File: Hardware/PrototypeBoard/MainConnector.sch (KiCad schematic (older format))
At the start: 13 parts, among them J3 ControlSupplyConnector

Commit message: Layout almost done
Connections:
- net ~GateDriverErr1: now also J3.9 (Pin_9); no longer J3.10 (Pin_10)
- net ~GateDriverErr2: now also J3.10 (Pin_10); no longer J3.9 (Pin_9)
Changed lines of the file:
@@
 Text HLabel 4500 2800 2    60   Output ~ 0
 GateDriverEna
+Text HLabel 3600 2700 0    60   Input ~ 0
+~GateDriverErr1
 Text HLabel 4500 2700 2    60   Input ~ 0
-~GateDriverErr1
-Text HLabel 3600 2700 0    60   Input ~ 0
 ~GateDriverErr2
 Text HLabel 4500 3200 2    60   Output ~ 0
@@
 	3800 4400 3700 4400
 Wire Wire Line
-	3700 4400 3700 5200
-Wire Wire Line
-	3600 4600 3800 4600
+	3700 4400 3700 4500
+Wire Wire Line
+	3600 4600 3700 4600
 Wire Wire Line
 	3800 4500 3700 4500
@@
 Connection ~ 3700 4600
 Wire Wire Line
-	3600 2300 3800 2300
-Wire Wire Line
-	3700 1700 3700 2500
+	3600 2300 3700 2300
+Wire Wire Line
+	3700 1700 3700 2000
 Wire Wire Line
 	3800 2400 3700 2400
 Connection ~ 3700 2400
 Wire Wire Line
-	4300 4600 7200 4600
-Wire Wire Line
-	4400 4400 4400 5200
+	4300 4600 4400 4600
+Wire Wire Line
+	4400 4400 4400 4500
 Wire Wire Line
 	4300 4500 4400 4500
@@
 	4300 2400 4400 2400
 Wire Wire Line
-	4300 4300 6000 4300
-Wire Wire Line
-	4300 2600 6000 2600
+	4300 4300 5900 4300
+Wire Wire Line
+	4300 2600 5800 2600
 Wire Wire Line
 	4400 4400 4300 4400
@@
 	4300 4000 4500 4000
 Wire Wire Line
-	4300 3900 6000 3900
+	4300 3900 5900 3900
 Wire Wire Line
 	4300 3800 4500 3800
@@
 	3600 4300 3800 4300
 Wire Wire Line
-	7600 2300 8200 2300
+	7600 2300 7900 2300
 Wire Wire Line
 	3600 5900 3600 6100
 Wire Wire Line
-	4400 1700 4400 2500
+	4400 1700 4400 2000
 Connection ~ 4400 2300
 Connection ~ 4400 2400
@@
 $EndComp
 Wire Wire Line
-	6300 2600 6700 2600
-Wire Wire Line
-	5900 2600 5900 4300
+	6300 2600 6500 2600
+Wire Wire Line
+	5900 2600 5900 3900
 Connection ~ 5900 2600
 Connection ~ 5900 3900
@@
 $EndComp
 Wire Wire Line
-	4300 2300 7300 2300
+	4300 2300 4400 2300
 Connection ~ 7000 2300
 $Comp
@@
 Text Notes 6550 2150 0    60   ~ 0
 TVS diode at \nthe PowerIn net\nburns the fuse in case \nDC link voltage rises \nover 30V during \nregenerative breaking
+Wire Wire Line
+	3700 4500 3700 4600
+Wire Wire Line
+	3700 4600 3800 4600
+Wire Wire Line
+	3700 4600 3700 4900
+Wire Wire Line
+	3700 2400 3700 2500
+Wire Wire Line
+	4400 4500 4400 4600
+Wire Wire Line
+	4400 4600 7200 4600
+Wire Wire Line
+	4400 4600 4400 4900
+Wire Wire Line
+	3700 2300 3800 2300
+Wire Wire Line
+	3700 2300 3700 2400
+Wire Wire Line
+	4400 2300 4400 2400
+Wire Wire Line
+	4400 2300 7000 2300
+Wire Wire Line
+	4400 2400 4400 2500
+Wire Wire Line
+	7200 2300 7300 2300
+Wire Wire Line
+	5900 2600 6000 2600
+Wire Wire Line
+	5900 3900 6000 3900
+Wire Wire Line
+	5900 3900 5900 4300
+Wire Wire Line
+	7900 2300 8200 2300
+Wire Wire Line
+	6500 2600 6700 2600
+Wire Wire Line
+	4400 4900 4400 5200
+Wire Wire Line
+	3700 4900 3700 5200
+Wire Wire Line
+	3700 2000 3700 2300
+Wire Wire Line
+	4400 2000 4400 2300
+Wire Wire Line
+	5900 4300 6000 4300
+Wire Wire Line
+	5800 2600 5900 2600
+Wire Wire Line
+	7000 2300 7200 2300
 $EndSCHEMATC

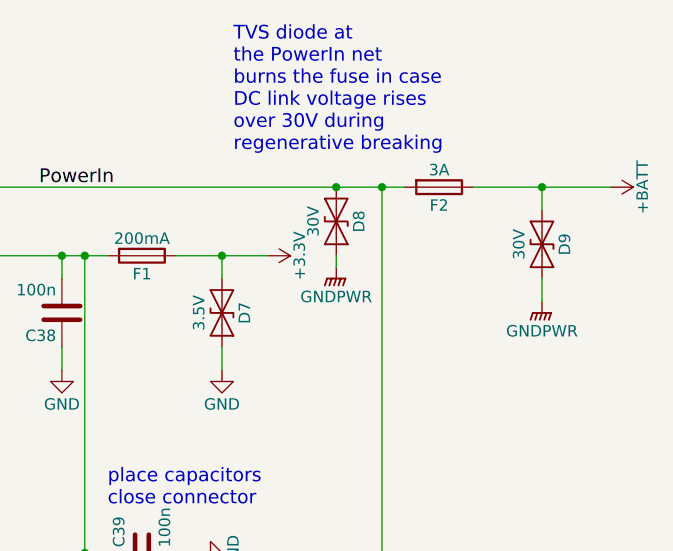
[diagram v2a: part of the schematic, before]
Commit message: Added LEDs for PWM, SPI communication, Gate Driver Errors and Gate Driver disabled
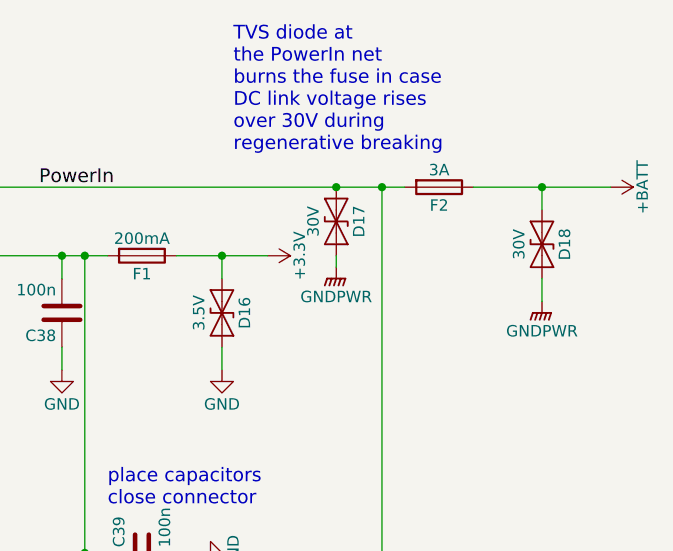
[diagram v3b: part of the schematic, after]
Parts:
- renumbered D7 to D16, D8 to D17, D9 to D18
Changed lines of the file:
@@
 $EndComp
 $Comp
-L PrototypeBoard-rescue:GNDPWR #PWR083
+L PrototypeBoard-rescue:GNDPWR #PWR089
 U 1 1 5AFFC52B
 P 3600 4600
-F 0 "#PWR083" H 3600 4400 50  0001 C CNN
+F 0 "#PWR089" H 3600 4400 50  0001 C CNN
 F 1 "GNDPWR" H 3600 4470 50  0000 C CNN
 F 2 "" H 3600 4550 50  0001 C CNN
@@
 $EndComp
 $Comp
-L PrototypeBoard-rescue:GNDPWR #PWR071
+L PrototypeBoard-rescue:GNDPWR #PWR077
 U 1 1 5AFFC541
 P 3600 2300
-F 0 "#PWR071" H 3600 2100 50  0001 C CNN
+F 0 "#PWR077" H 3600 2100 50  0001 C CNN
 F 1 "GNDPWR" H 3600 2170 50  0000 C CNN
 F 2 "" H 3600 2250 50  0001 C CNN
@@
 $EndComp
 $Comp
-L power:+BATT #PWR095
+L power:+BATT #PWR0101
 U 1 1 5AFFC5BD
 P 8200 2300
-F 0 "#PWR095" H 8200 2150 50  0001 C CNN
+F 0 "#PWR0101" H 8200 2150 50  0001 C CNN
 F 1 "+BATT" H 8200 2440 50  0000 C CNN
 F 2 "" H 8200 2300 50  0001 C CNN
@@
 $EndComp
 $Comp
-L power:GND #PWR072
+L power:GND #PWR078
 U 1 1 5AFFC6F4
 P 3600 2600
-F 0 "#PWR072" H 3600 2350 50  0001 C CNN
+F 0 "#PWR078" H 3600 2350 50  0001 C CNN
 F 1 "GND" H 3600 2450 50  0000 C CNN
 F 2 "" H 3600 2600 50  0001 C CNN
@@
 $EndComp
 $Comp
-L power:GND #PWR082
+L power:GND #PWR088
 U 1 1 5AFFC70F
 P 3600 4300
-F 0 "#PWR082" H 3600 4050 50  0001 C CNN
+F 0 "#PWR088" H 3600 4050 50  0001 C CNN
 F 1 "GND" H 3600 4150 50  0000 C CNN
 F 2 "" H 3600 4300 50  0001 C CNN
@@
 $EndComp
 $Comp
-L power:+3.3V #PWR092
+L power:+3.3V #PWR098
 U 1 1 5AFFC799
 P 6700 2600
-F 0 "#PWR092" H 6700 2450 50  0001 C CNN
+F 0 "#PWR098" H 6700 2450 50  0001 C CNN
 F 1 "+3.3V" H 6700 2740 50  0000 C CNN
 F 2 "" H 6700 2600 50  0001 C CNN
@@
 $EndComp
 $Comp
-L power:GND #PWR081
+L power:GND #PWR087
 U 1 1 5AFFCA44
 P 3600 4100
-F 0 "#PWR081" H 3600 3850 50  0001 C CNN
+F 0 "#PWR087" H 3600 3850 50  0001 C CNN
 F 1 "GND" H 3600 3950 50  0000 C CNN
 F 2 "" H 3600 4100 50  0001 C CNN
@@
 $EndComp
 $Comp
-L power:GND #PWR080
+L power:GND #PWR086
 U 1 1 5AFFCA52
 P 3600 4000
-F 0 "#PWR080" H 3600 3750 50  0001 C CNN
+F 0 "#PWR086" H 3600 3750 50  0001 C CNN
 F 1 "GND" H 3600 3850 50  0000 C CNN
 F 2 "" H 3600 4000 50  0001 C CNN
@@
 $EndComp
 $Comp
-L power:GND #PWR079
+L power:GND #PWR085
 U 1 1 5AFFCA60
 P 3600 3900
-F 0 "#PWR079" H 3600 3650 50  0001 C CNN
+F 0 "#PWR085" H 3600 3650 50  0001 C CNN
 F 1 "GND" H 3600 3750 50  0000 C CNN
 F 2 "" H 3600 3900 50  0001 C CNN
@@
 $EndComp
 $Comp
-L power:GND #PWR078
+L power:GND #PWR084
 U 1 1 5AFFCA6E
 P 3600 3700
-F 0 "#PWR078" H 3600 3450 50  0001 C CNN
+F 0 "#PWR084" H 3600 3450 50  0001 C CNN
 F 1 "GND" H 3600 3550 50  0000 C CNN
 F 2 "" H 3600 3700 50  0001 C CNN
@@
 $EndComp
 $Comp
-L power:GND #PWR077
+L power:GND #PWR083
 U 1 1 5AFFCA7C
 P 3600 3600
-F 0 "#PWR077" H 3600 3350 50  0001 C CNN
+F 0 "#PWR083" H 3600 3350 50  0001 C CNN
 F 1 "GND" H 3600 3450 50  0000 C CNN
 F 2 "" H 3600 3600 50  0001 C CNN
@@
 $EndComp
 $Comp
-L power:GND #PWR076
+L power:GND #PWR082
 U 1 1 5AFFCA98
 P 3600 3500
-F 0 "#PWR076" H 3600 3250 50  0001 C CNN
+F 0 "#PWR082" H 3600 3250 50  0001 C CNN
 F 1 "GND" H 3600 3350 50  0000 C CNN
 F 2 "" H 3600 3500 50  0001 C CNN
@@
 $EndComp
 $Comp
-L power:GND #PWR075
+L power:GND #PWR081
 U 1 1 5AFFCAA6
 P 3600 3400
-F 0 "#PWR075" H 3600 3150 50  0001 C CNN
+F 0 "#PWR081" H 3600 3150 50  0001 C CNN
 F 1 "GND" H 3600 3250 50  0000 C CNN
 F 2 "" H 3600 3400 50  0001 C CNN
@@
 $EndComp
 $Comp
-L power:GND #PWR074
+L power:GND #PWR080
 U 1 1 5AFFCAB4
 P 3600 3200
-F 0 "#PWR074" H 3600 2950 50  0001 C CNN
+F 0 "#PWR080" H 3600 2950 50  0001 C CNN
 F 1 "GND" H 3600 3050 50  0000 C CNN
 F 2 "" H 3600 3200 50  0001 C CNN
@@
 $EndComp
 $Comp
-L power:+3.3V #PWR084
+L power:+3.3V #PWR090
 U 1 1 5AFF6F2E
 P 3600 5900
-F 0 "#PWR084" H 3600 5750 50  0001 C CNN
+F 0 "#PWR090" H 3600 5750 50  0001 C CNN
 F 1 "+3.3V" H 3600 6040 50  0000 C CNN
 F 2 "" H 3600 5900 50  0001 C CNN
@@
 $EndComp
 $Comp
-L power:+BATT #PWR085
+L power:+BATT #PWR091
 U 1 1 5AFF72BB
 P 4100 5900
-F 0 "#PWR085" H 4100 5750 50  0001 C CNN
+F 0 "#PWR091" H 4100 5750 50  0001 C CNN
 F 1 "+BATT" H 4100 6040 50  0000 C CNN
 F 2 "" H 4100 5900 50  0001 C CNN
@@
 	4100 5900 4100 6100
 $Comp
-L power:GND #PWR086
+L power:GND #PWR092
 U 1 1 5AFF731E
 P 4600 6100
-F 0 "#PWR086" H 4600 5850 50  0001 C CNN
+F 0 "#PWR092" H 4600 5850 50  0001 C CNN
 F 1 "GND" H 4600 5950 50  0000 C CNN
 F 2 "" H 4600 6100 50  0001 C CNN
@@
 $EndComp
 $Comp
-L PrototypeBoard-rescue:GNDPWR #PWR087
+L PrototypeBoard-rescue:GNDPWR #PWR093
 U 1 1 5AFF7385
 P 5100 6100
-F 0 "#PWR087" H 5100 5900 50  0001 C CNN
+F 0 "#PWR093" H 5100 5900 50  0001 C CNN
 F 1 "GNDPWR" H 5100 5970 50  0000 C CNN
 F 2 "" H 5100 6050 50  0001 C CNN
@@
 	4300 2800 4500 2800
 $Comp
-L power:GND #PWR073
+L power:GND #PWR079
 U 1 1 5AFF86D9
 P 3600 2800
-F 0 "#PWR073" H 3600 2550 50  0001 C CNN
+F 0 "#PWR079" H 3600 2550 50  0001 C CNN
 F 1 "GND" H 3600 2650 50  0000 C CNN
 F 2 "" H 3600 2800 50  0001 C CNN
@@
 Since ERC complains about no drivers in power net \n(connector pins don't have the type "Power Output"), \nthis workaround has to be used
 $Comp
-L PrototypeBoard-rescue:GNDPWR #PWR094
+L PrototypeBoard-rescue:GNDPWR #PWR0100
 U 1 1 5B0080B7
 P 7900 2800
-F 0 "#PWR094" H 7900 2600 50  0001 C CNN
+F 0 "#PWR0100" H 7900 2600 50  0001 C CNN
 F 1 "GNDPWR" H 7900 2670 50  0000 C CNN
 F 2 "" H 7900 2750 50  0001 C CNN
@@
 Connection ~ 5900 3900
 $Comp
-L power:GND #PWR091
+L power:GND #PWR097
 U 1 1 5B008FFB
 P 6500 3100
-F 0 "#PWR091" H 6500 2850 50  0001 C CNN
+F 0 "#PWR097" H 6500 2850 50  0001 C CNN
 F 1 "GND" H 6500 2950 50  0000 C CNN
 F 2 "" H 6500 3100 50  0001 C CNN
@@
 $EndComp
 $Comp
-L Device:D_TVS D9
+L Device:D_TVS D18
 U 1 1 5B00D2A4
 P 7900 2550
-F 0 "D9" H 7900 2650 50  0000 C CNN
+F 0 "D18" H 7900 2650 50  0000 C CNN
 F 1 "30V" H 7900 2450 50  0000 C CNN
 F 2 "Diodes_SMD:D_SMA-SMB_Universal_Handsoldering" H 7900 2550 50  0001 C CNN
@@
 	7900 2700 7900 2800
 $Comp
-L Device:D_TVS D7
+L Device:D_TVS D16
 U 1 1 5B00D572
 P 6500 2850
-F 0 "D7" H 6500 2950 50  0000 C CNN
+F 0 "D16" H 6500 2950 50  0000 C CNN
 F 1 "3.5V" H 6500 2750 50  0000 C CNN
 F 2 "Diodes_SMD:D_SOD-323_HandSoldering" H 6500 2850 50  0001 C CNN
@@
 Connection ~ 5900 4300
 $Comp
-L power:GND #PWR089
+L power:GND #PWR095
 U 1 1 5B00DFF3
 P 6400 3900
-F 0 "#PWR089" H 6400 3650 50  0001 C CNN
+F 0 "#PWR095" H 6400 3650 50  0001 C CNN
 F 1 "GND" H 6400 3750 50  0000 C CNN
 F 2 "" H 6400 3900 50  0001 C CNN
@@
 $EndComp
 $Comp
-L power:GND #PWR090
+L power:GND #PWR096
 U 1 1 5B00E052
 P 6400 4300
-F 0 "#PWR090" H 6400 4050 50  0001 C CNN
+F 0 "#PWR096" H 6400 4050 50  0001 C CNN
 F 1 "GND" H 6400 4150 50  0000 C CNN
 F 2 "" H 6400 4300 50  0001 C CNN
@@
 Connection ~ 5800 2600
 $Comp
-L power:GND #PWR088
+L power:GND #PWR094
 U 1 1 5B00E24D
 P 5800 3100
-F 0 "#PWR088" H 5800 2850 50  0001 C CNN
+F 0 "#PWR094" H 5800 2850 50  0001 C CNN
 F 1 "GND" H 5800 2950 50  0000 C CNN
 F 2 "" H 5800 3100 50  0001 C CNN
@@
 3V3in
 $Comp
-L Device:D_TVS D8
+L Device:D_TVS D17
 U 1 1 5B27A7EB
 P 7000 2450
-F 0 "D8" H 7000 2550 50  0000 C CNN
+F 0 "D17" H 7000 2550 50  0000 C CNN
 F 1 "30V" H 7000 2350 50  0000 C CNN
 F 2 "Diodes_SMD:D_SMA-SMB_Universal_Handsoldering" H 7000 2450 50  0001 C CNN
@@
 Connection ~ 7000 2300
 $Comp
-L PrototypeBoard-rescue:GNDPWR #PWR093
+L PrototypeBoard-rescue:GNDPWR #PWR099
 U 1 1 5B27AA44
 P 7000 2650
-F 0 "#PWR093" H 7000 2450 50  0001 C CNN
+F 0 "#PWR099" H 7000 2450 50  0001 C CNN
 F 1 "GNDPWR" H 7000 2520 50  0000 C CNN
 F 2 "" H 7000 2600 50  0001 C CNN
